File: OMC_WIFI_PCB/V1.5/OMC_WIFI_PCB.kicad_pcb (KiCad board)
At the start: 2 copper layers, 106.8 x 66.8 mm, 26 parts, among them J1 Conn_01x02_Male, J10 Conn_01x01_Male, J2 Conn_01x02_Female, J3 Conn_01x02_Male, J4 Switch, J5 Pins_FT232R, J6 Level shifter, J7 Conn_01x01_Female, J8 Regulador, J9 Conn_01x01_Female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

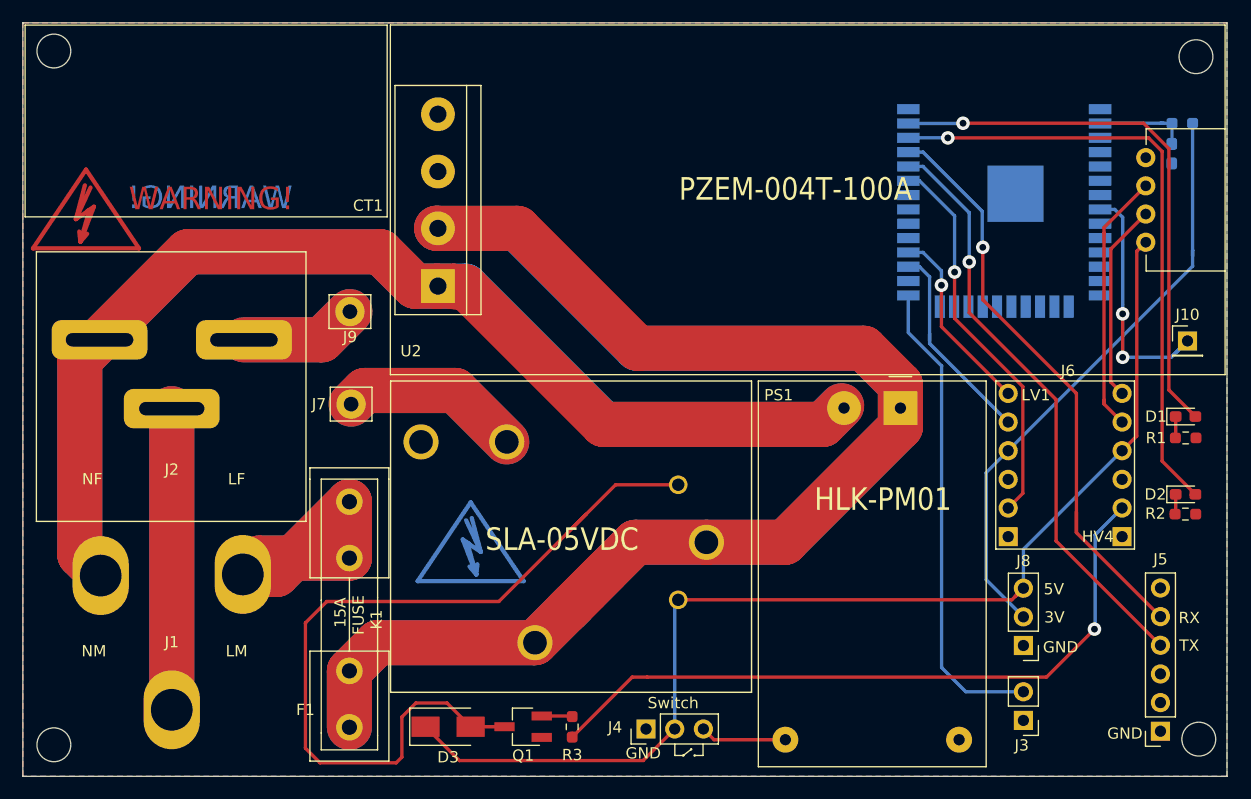
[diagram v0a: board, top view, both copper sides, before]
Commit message: Actualización PCB
> Cambio en polaridad de transistor
> Cambio en planos de tierra y B.Mask
> Cambio en librería de conector hembra AC
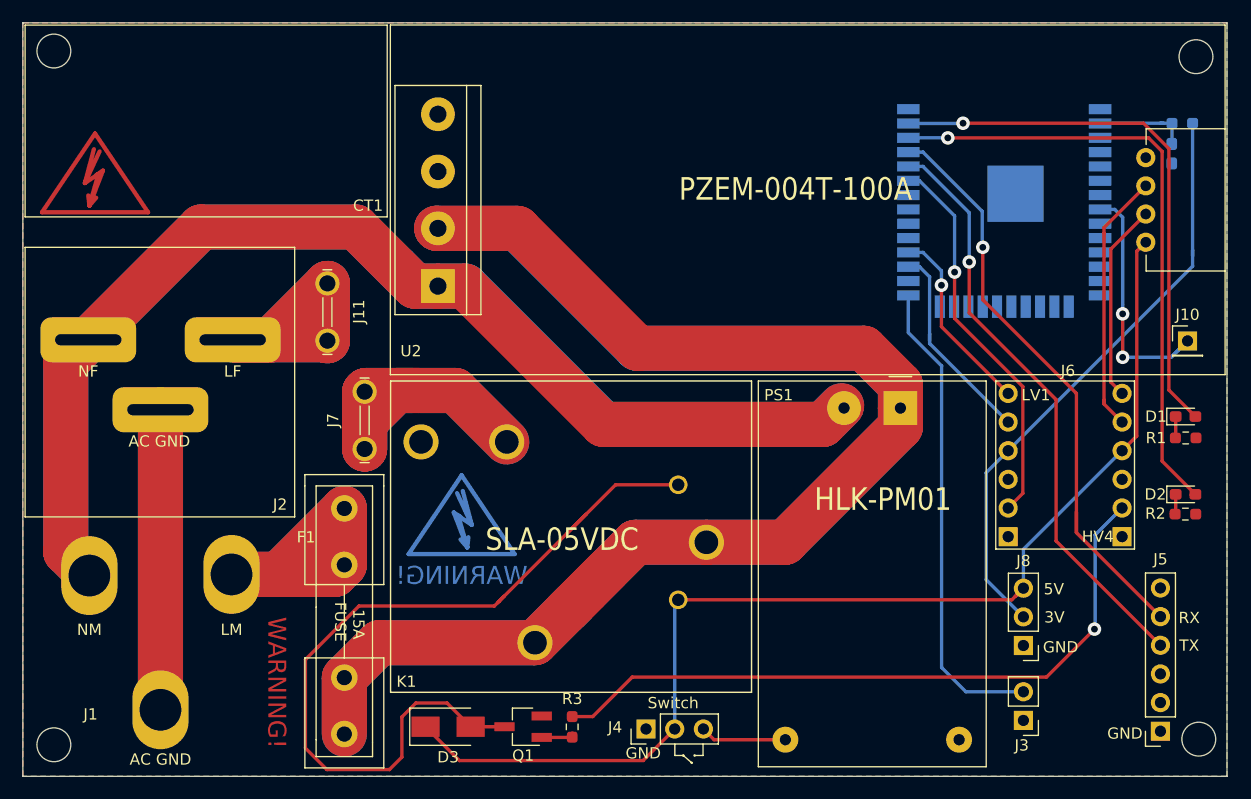
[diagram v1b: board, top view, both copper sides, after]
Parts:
- removed J9: Conn_01x01_Female, Connector_Pin:Pin_D1.3mm_L10.0mm_W3.5mm_Flat
- added J11: 62409-1, conector_espada:espada, F.Cu at (603.0, -955.9)
- J7: value Conn_01x01_Female -> 62409-1; footprint Connector_Pin:Pin_D1.3mm_L10.0mm_W3.5mm_Flat -> conector_espada:espada
- moved SYM1 3.30 mm to (582.4, -967.5)
- moved SYM2 2.53 mm to (614.9, -937.2)
- moved J7 1.87 mm to (606.3, -946.3), turned to 90 degrees
- moved J1 1.00 mm to (588.2, -932.5)
- moved J2 1.00 mm to (588.2, -953.4)
- moved F1 0.75 mm to (604.5, -918.5)
- turned R3 to 270 degrees
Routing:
- net Net-(J11-Pad1): track 20.9 -> 48.0 mm
- net LINE_OUT: track 32.4 -> 55.3 mm
- net NEUTRAL: track 197.1 -> 205.1 mm
- net LINE_IN: track 236.6 -> 238.0 mm
- net Net-(F1-Pad2): track 54.3 -> 55.6 mm
- net D32_RELAY_5V: track 62.4 -> 61.3 mm
- net Net-(D3-Pad2): track 74.9 -> 74.4 mm
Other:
- board text added: "AC GND"

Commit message: Creación de GERBERS PCB v1.5
Se incluyen cambios pequeños en la PCB:
> Cambio al transistor MMBT3904
> Cambio en puntos de soldadura para los cables del toroide.
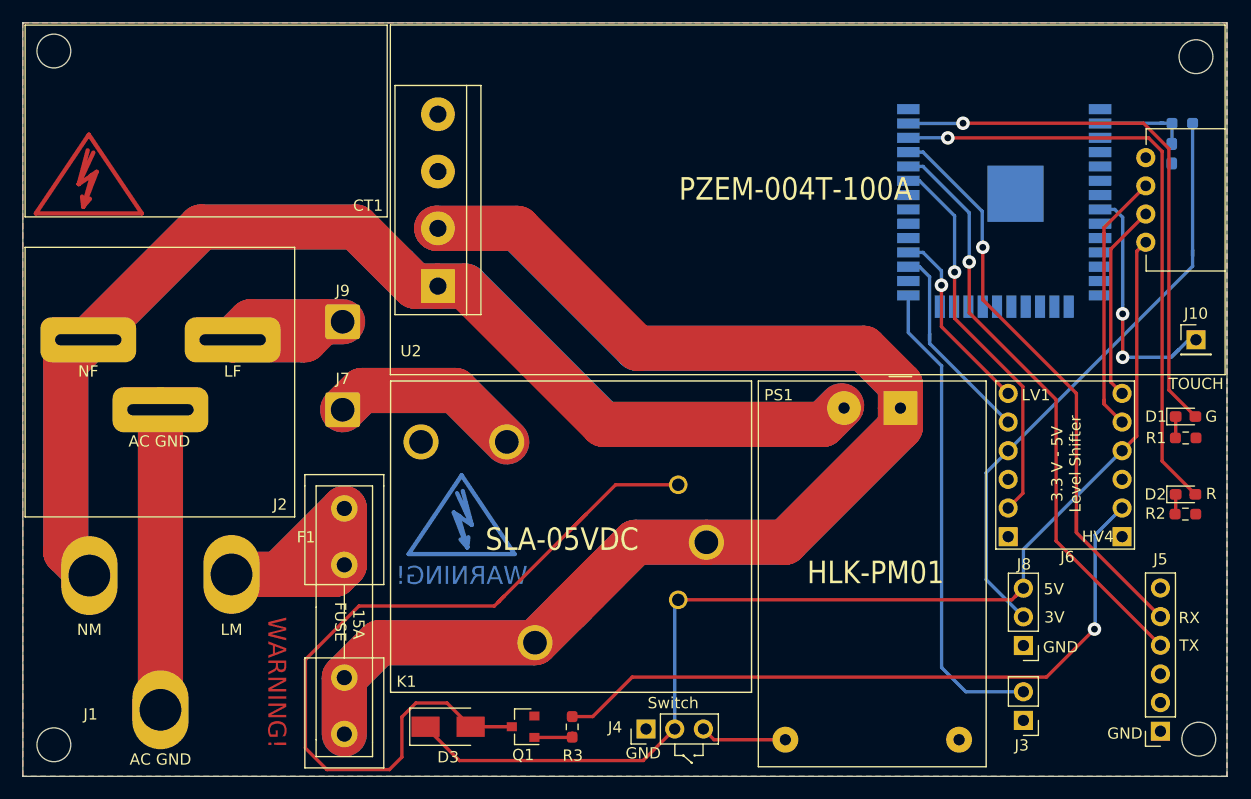
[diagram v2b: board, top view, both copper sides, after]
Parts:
- removed J11: 62409-1, conector_espada:espada
- added J9: Conn_01x01_Female, Connector_Wire:SolderWire-1.5sqmm_1x01_D1.7mm_OD3mm, F.Cu at (604.4, -955.0)
- J7: value 62409-1 -> Conn_01x01_Female; footprint conector_espada:espada -> Connector_Wire:SolderWire-1.5sqmm_1x01_D1.7mm_OD3mm
- Q1: value 2N3904 -> MMBT3904; footprint Package_TO_SOT_SMD:SC-59_Handsoldering -> Package_TO_SOT_SMD:SOT-23
- moved J7 2.16 mm to (604.4, -947.2), turned to 0 degrees
- moved J10 0.76 mm to (680.0, -953.4)
- moved SYM1 0.56 mm to (581.9, -967.4)
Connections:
- Q1 pad 1: GND -> Net-(Q1-Pad1)
- Q1 pad 2: Net-(Q1-Pad2) -> GND
- R3 pad 2: Net-(Q1-Pad2) -> Net-(Q1-Pad1)
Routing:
- net LINE_OUT: track 55.3 -> 34.3 mm
- net Net-(J2-Pad1): track 48.0 -> 38.0 mm
- net Net-(Q1-Pad1): track 0.00 -> 3.73 mm
- net Net-(Q1-Pad2): track 3.08 -> 0.00 mm
- net Net-(D3-Pad2): track 74.4 -> 75.0 mm
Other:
- board text added: "3.3 V - 5V Level Shifter"
- board text added: "G"
- board text added: "R"
- board text added: "TOUCH"
